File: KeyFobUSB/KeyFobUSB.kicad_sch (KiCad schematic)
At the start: 17 parts, among them J1 USB_A, SW2 SW_SPDT, U1 ATtiny85V-10S

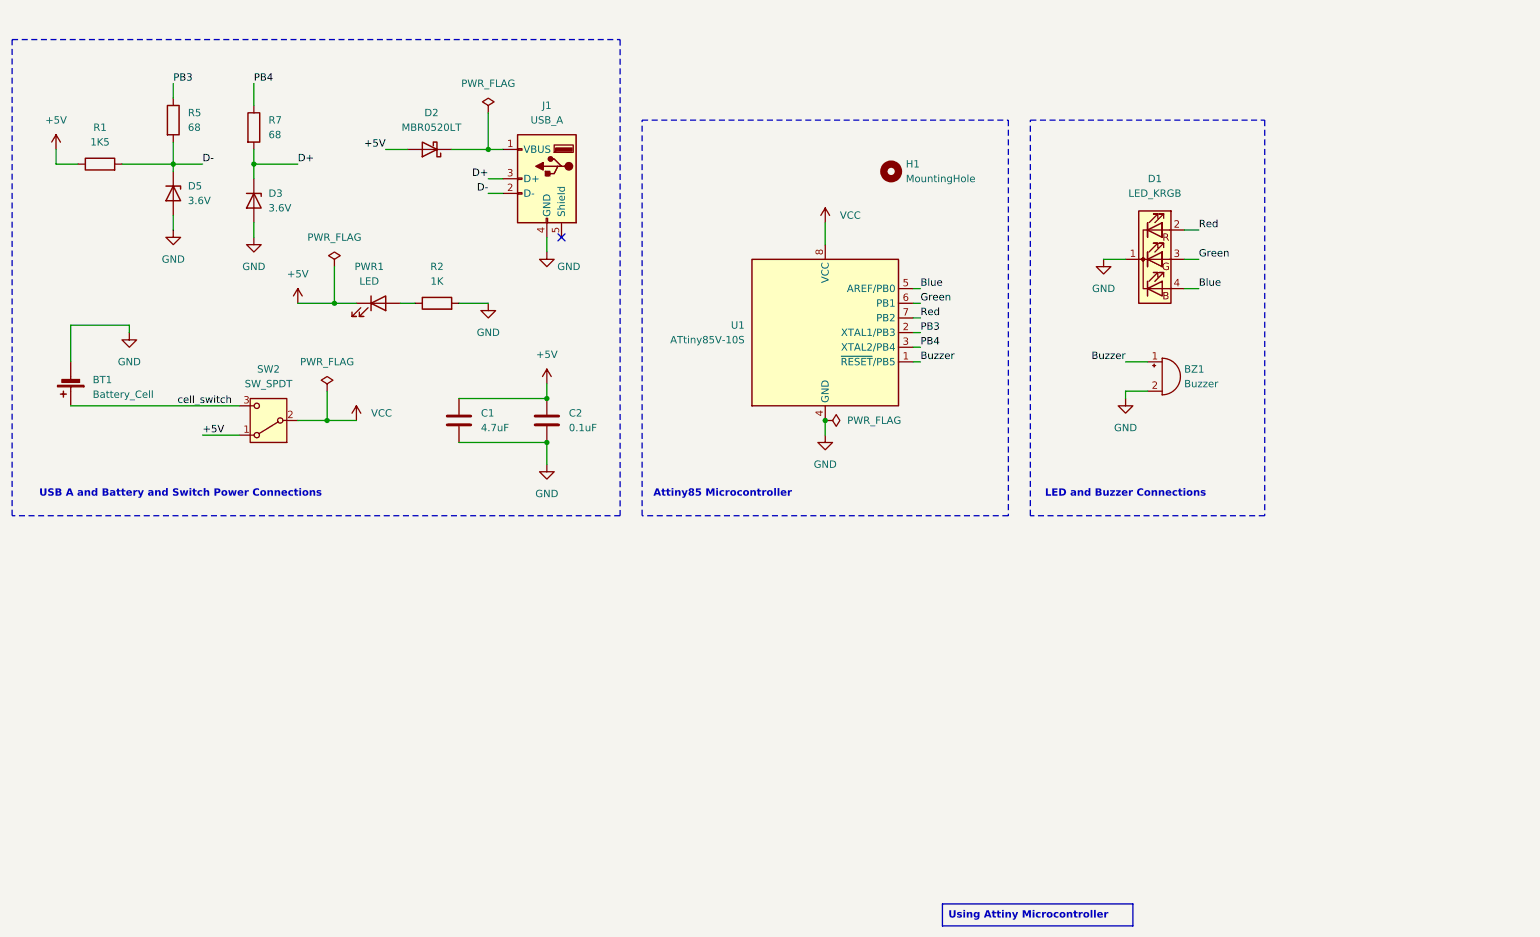
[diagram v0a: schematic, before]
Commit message: Completed the schematic and placed the components on pcb
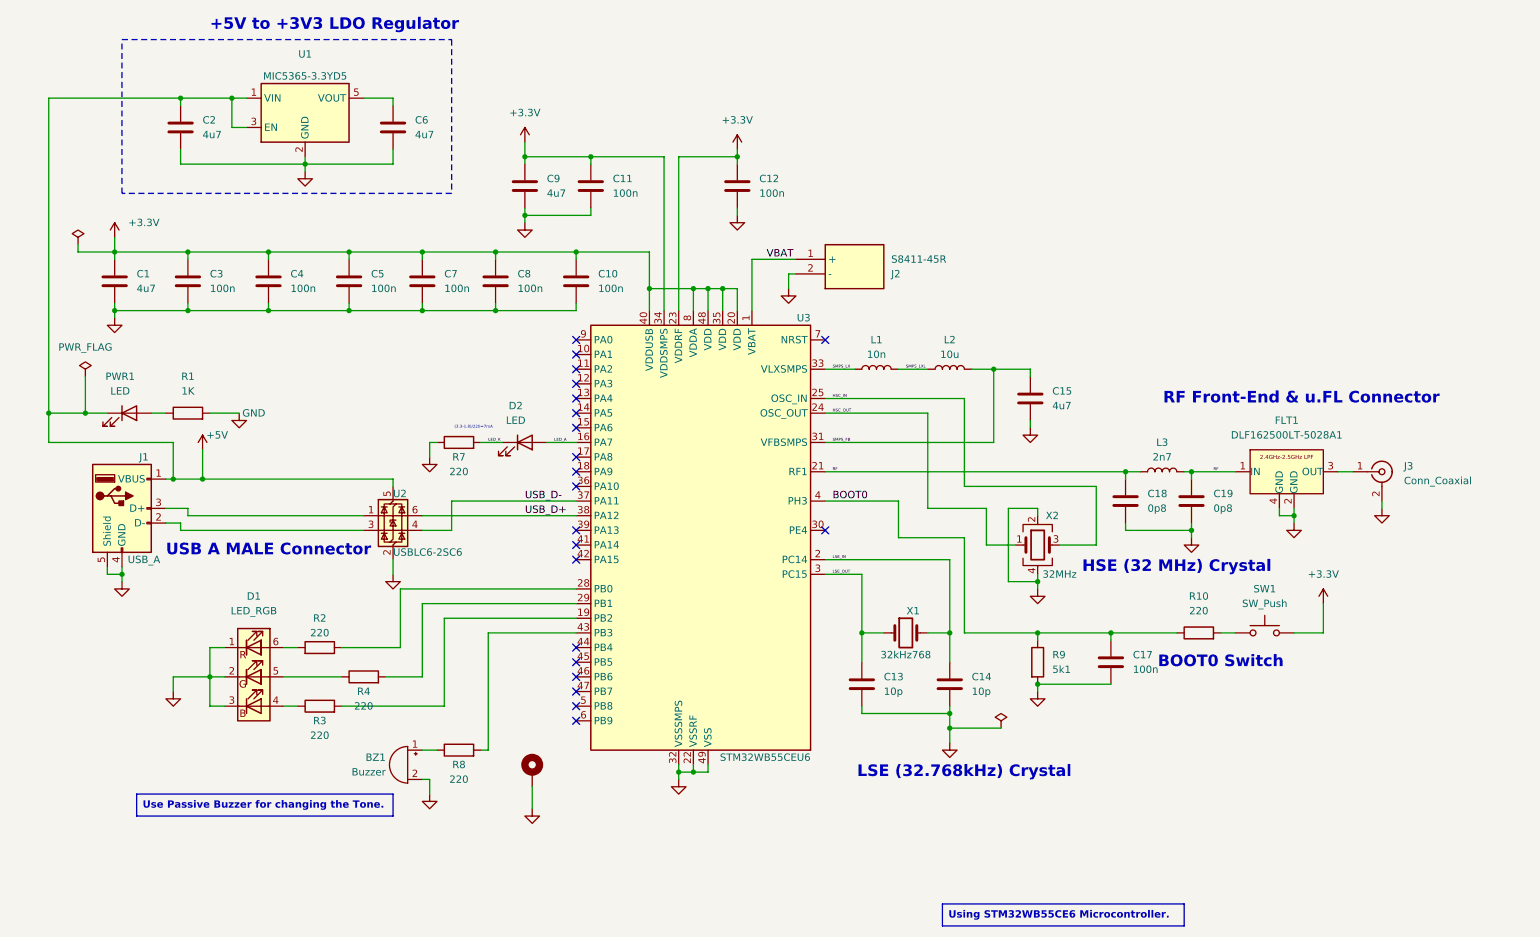
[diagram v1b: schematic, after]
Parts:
- removed BT1: Battery_Cell, 22BatteryHoldercoincell_S8411-45R:S8411-45R_1, symbol Device:Battery_Cell
- removed D1: LED_KRGB, LED_THT:LED_D5.0mm-4_RGB, symbol Device:LED_KRGB
- removed D2: MBR0520LT, Diode_SMD:D_SOD-123, symbol Diode:MBR0520LT
- removed D3, D5: 3.6V, Diode_SMD:D_1206_3216Metric, symbol Device:D_Zener
- removed H1: MountingHole, MountingHole:MountingHole_4.3mm_M4, symbol Mechanical:MountingHole
- removed R1: 1K5, Resistor_SMD:R_0805_2012Metric, symbol Device:R
- removed R5: 68, Resistor_SMD:R_0805_2012Metric, symbol Device:R
- removed SW2: SW_SPDT, Button_Switch_SMD:SW_SPDT_PCM12, symbol Switch:SW_SPDT
- removed U1: ATtiny85V-10S, Package_SO:SOIC-8W_5.3x5.3mm_P1.27mm, symbol MCU_Microchip_ATtiny:ATtiny85V-10S
- added C10, C11, C12, C17, C3, C4, C5, C7, C8: 100n, Capacitor_SMD:C_0805_2012Metric, symbol Device:C
- added C13, C14: 10p, Capacitor_SMD:C_0805_2012Metric, symbol Device:C
- added C15, C6, C9: 4u7, Capacitor_SMD:C_0805_2012Metric, symbol Device:C
- added C18, C19: 0p8, Capacitor_SMD:C_0805_2012Metric, symbol Device:C
- added D1: LED_RGB, LED_SMD:LED_Inolux_IN-P55TATRGB_PLCC6_5.0x5.5mm_P1.8mm, symbol Device:LED_RGB
- added D2: LED, LED_SMD:LED_0805_2012Metric, symbol Device:LED
- added FLT1: DLF162500LT-5028A1, DLF162500LT-5028A1:DLF162500LT-5028A1, symbol STM32withBle_SchematicSymbol:DLF162500LT-5028A1
- added H+1: MountingHole_Pad, MountingHole:MountingHole_3mm_Pad_Via, symbol Mechanical:MountingHole_Pad
- added J2: S8411-45R, 22BatteryHoldercoincell_S8411-45R:S8411-45R_1, symbol battery holder S8411-45R:S8411-45R
- added J3: Conn_Coaxial, Connector_Coaxial:U.FL_Hirose_U.FL-R-SMT-1_Vertical, symbol Connector:Conn_Coaxial
- added L1: 10n, Inductor_SMD:L_0805_2012Metric, symbol Device:L
- added L2: 10u, Inductor_SMD:L_0805_2012Metric, symbol Device:L
- added L3: 2n7, Inductor_SMD:L_0805_2012Metric, symbol Device:L
- added R10, R2, R3, R4, R8: 220, Resistor_SMD:R_0805_2012Metric, symbol Device:R
- added R9: 5k1, Resistor_SMD:R_0805_2012Metric, symbol Device:R
- added SW1: SW_Push, Button_Switch_SMD:SW_SPST_CK_RS282G05A3, symbol Switch:SW_Push
- added U1: MIC5365-3.3YD5, Package_TO_SOT_SMD:SOT-23-5, symbol Regulator_Linear:MIC5365-3.3YD5
- added U2: USBLC6-2SC6, Package_TO_SOT_SMD:SOT-23-6, symbol Power_Protection:USBLC6-2SC6
- added U3: STM32WB55CEU6, Package_DFN_QFN:QFN-48-1EP_7x7mm_P0.5mm_EP5.6x5.6mm, symbol MCU_ST_STM32WB:STM32WB55CEUx
- added X1: 32kHz768, Crystal:Crystal_SMD_2012-2Pin_2.0x1.2mm, symbol Device:Crystal
- added X2: 32MHz, Crystal:Crystal_SMD_2016-4Pin_2.0x1.6mm, symbol Device:Crystal_GND24
- BZ1: footprint Buzzer_Beeper:MagneticBuzzer_ProSignal_ABT-410-RC -> Buzzer_Beeper:Buzzer_CUI_CPT-9019S-SMT
- C1: value 4.7uF -> 4u7
- C2: value 0.1uF -> 4u7
- J1: now left out of the parts list
- R7: value 68 -> 220
- renumbered R2 to R1
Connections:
- net PB4 is gone; now on net GND: R7.1
- net +5V: now also J1.1 (VBUS), U1.1 (VIN), U1.3 (EN), U2.5 (VBUS); no longer C1.1
- net GND: now also J1.5 (Shield), C10.2, C11.2, C12.2, C13.2, C14.2, C15.2, C17.2, C18.2, C19.2, C3.2, C4.2, C5.2, C6.2, C7.2, C8.2, C9.2, D1.1 (RK), D1.2 (GK), D1.3 (BK), FLT1.2 (GND), FLT1.4 (GND), H+1.1, J2.2 (-), J3.2 (Ext), R9.2, U1.2 (GND), U2.2 (GND), U3.22 (VSSRF), U3.32 (VSSSMPS), U3.49 (VSS), X2.2, X2.4
- net Buzzer: no longer names the net of BZ1.1 (+)
- net Buzzer: now also R8.1
- net D+: no longer names the net of J1.3 (D+)
- net D+: now also U2.1 (I/O1); no longer R7.2
- net D-: no longer names the net of J1.2 (D-)
- net D-: now also U2.3 (I/O2)
- new net: D1.4 (BA), R3.1
- new net: D1.5 (GA), R4.1
- new net: D1.6 (RA), R2.2
- new net: R4.2, U3.29 (PB1)
- new net: FLT1.3 (OUT), J3.1 (In)
- new net: C6.1, U1.5 (VOUT)
- new net: R10.2, SW1.1
- new net: R8.2, U3.43 (PB3)
- new net: R2.1, U3.28 (PB0)
- new net: R3.2, U3.19 (PB2)
- new net +3.3V: C1.1, C10.1, C11.1, C12.1, C3.1, C4.1, C5.1, C7.1, C8.1, C9.1, SW1.2, U3.20 (VDD), U3.23 (VDDRF), U3.34 (VDDSMPS), U3.35 (VDD), U3.40 (VDDUSB), U3.48 (VDD), U3.8 (VDDA)
- new net BOOT0: C17.1, R10.1, R9.1, U3.4 (PH3)
- new net HSC_IN: U3.25 (OSC_IN), X2.3
- new net HSC_OUT: U3.24 (OSC_OUT), X2.1
- new net LED_A: D2.2 (A), U3.16 (PA7)
- new net LED_K: D2.1 (K), R7.2
- new net LSE_IN: C14.1, U3.2 (PC14), X1.2
- new net LSE_OUT: C13.1, U3.3 (PC15), X1.1
- new net RF: C18.1, C19.1, FLT1.1 (IN), L3.1, L3.2, U3.21 (RF1)
- new net SMPS_FB: C15.1, L2.2, U3.31 (VFBSMPS)
- new net SMPS_LX: L1.1, U3.33 (VLXSMPS)
- new net SMPS_LXL: L1.2, L2.1
- new net USB_D+: U2.6 (I/O1), U3.38 (PA12)
- new net USB_D-: U2.4 (I/O2), U3.37 (PA11)
- new net VBAT: J2.1 (+), U3.1 (VBAT)
- no-connect marks 1 -> 21
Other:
- note added: "(3.3-1.8)/220=7mA"
- note added: "+5V to +3V3 LDO Regulator"
- note added: "BOOT0 Switch"
- note added: "HSE (32 MHz) Crystal"
- note added: "LSE (32.768kHz) Crystal"
- note added: "RF Front-End & u.FL Connector"
- note added: "USB A MALE Connector"
- note removed: "Attiny85 Microcontroller"
- note removed: "LED and Buzzer Connections"
- note removed: "USB A and Battery and Switch Power Connections"
- moved on the sheet: J1, PWR1, R1

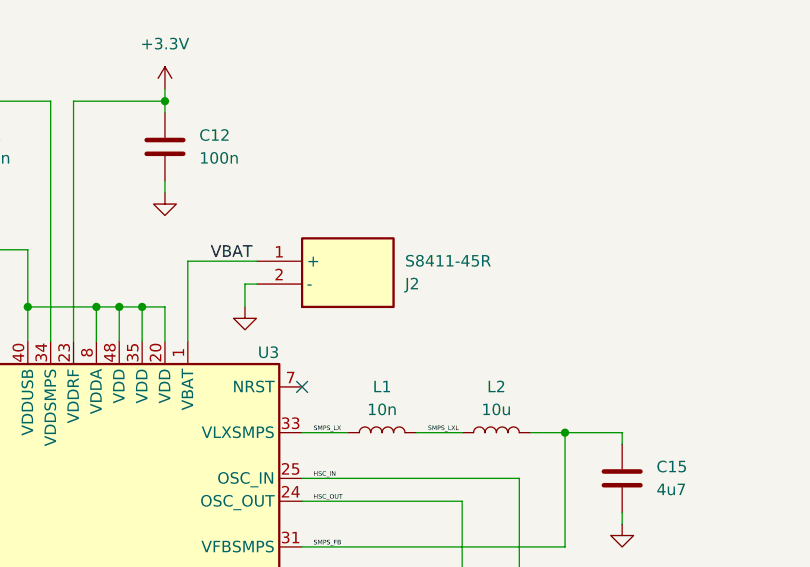
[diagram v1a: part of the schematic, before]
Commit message: added battery holder and vias
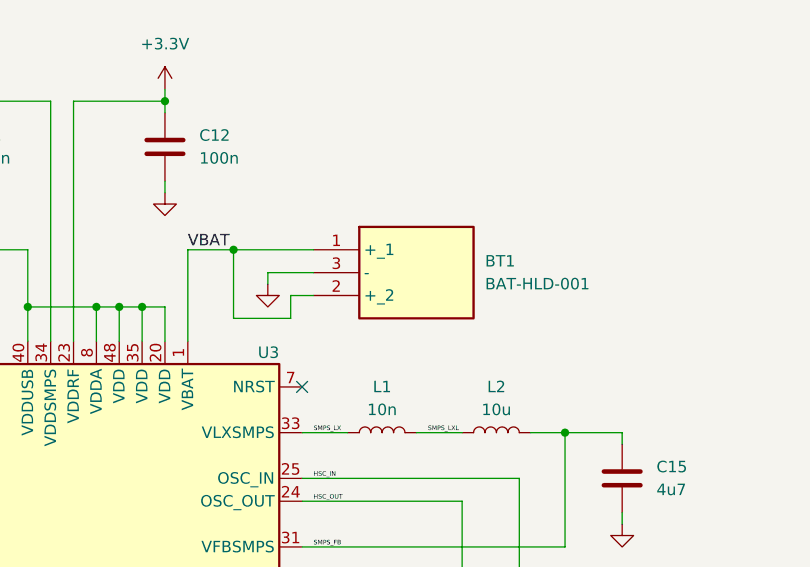
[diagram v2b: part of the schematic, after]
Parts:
- removed J2: S8411-45R, 22BatteryHoldercoincell_S8411-45R:S8411-45R_1, symbol battery holder S8411-45R:S8411-45R
- added BT1: BAT-HLD-001, 22BatteryHoldercoincell_S8411-45R:BATHLD001 CR2032, symbol battery Holder CR2032 001:BAT-HLD-001
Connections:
- net GND: now also BT1.3 (-)
- net VBAT: now also BT1.1 (+_1), BT1.2 (+_2)
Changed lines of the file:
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@@
 	)
 	(junction
+		(at 151.13 54.61)
+		(diameter 0)
+		(color 0 0 0 0)
+	)
+	(junction
 		(at 106.68 38.1)
 		(diameter 0)
@@
 	(wire
 		(pts
-			(xy 146.05 55.88) (xy 146.05 64.77)
+			(xy 146.05 54.61) (xy 146.05 64.77)
 		)
 		(stroke
@@
 	(wire
 		(pts
+			(xy 151.13 62.23) (xy 151.13 54.61)
+		)
+		(stroke
+			(width 0)
+			(type default)
+		)
+	)
+	(wire
+		(pts
 			(xy 88.9 63.5) (xy 88.9 64.77)
 		)
@@
 	(wire
 		(pts
+			(xy 157.48 59.69) (xy 160.02 59.69)
+		)
+		(stroke
+			(width 0)
+			(type default)
+		)
+	)
+	(wire
+		(pts
 			(xy 135.89 60.96) (xy 128.27 60.96)
 		)
@@
 	(wire
 		(pts
-			(xy 153.67 58.42) (xy 152.4 58.42)
+			(xy 154.94 57.15) (xy 160.02 57.15)
 		)
 		(stroke
@@
 	(wire
 		(pts
-			(xy 152.4 58.42) (xy 152.4 60.96)
+			(xy 154.94 57.15) (xy 154.94 58.42)
 		)
 		(stroke
@@
 	(wire
 		(pts
+			(xy 157.48 62.23) (xy 151.13 62.23)
+		)
+		(stroke
+			(width 0)
+			(type default)
+		)
+	)
+	(wire
+		(pts
 			(xy 210.82 93.98) (xy 210.82 92.71)
 		)
@@
 	(wire
 		(pts
+			(xy 151.13 54.61) (xy 160.02 54.61)
+		)
+		(stroke
+			(width 0)
+			(type default)
+		)
+	)
+	(wire
+		(pts
 			(xy 180.34 134.62) (xy 180.34 137.16)
 		)
@@
 	(wire
 		(pts
+			(xy 157.48 59.69) (xy 157.48 62.23)
+		)
+		(stroke
+			(width 0)
+			(type default)
+		)
+	)
+	(wire
+		(pts
 			(xy 52.07 133.35) (xy 52.07 128.27)
 		)
@@
 	(wire
 		(pts
-			(xy 153.67 55.88) (xy 146.05 55.88)
+			(xy 146.05 54.61) (xy 151.13 54.61)
 		)
 		(stroke
@@
 	)
 	(label "VBAT"
-		(at 148.59 55.88 0)
+		(at 146.05 54.61 0)
 		(fields_autoplaced yes)
 		(effects
@@
 	)
 	(symbol
-		(lib_id "battery holder S8411-45R:S8411-45R")
-		(at 153.67 58.42 0)
-		(mirror x)
-		(unit 1)
-		(exclude_from_sim no)
-		(in_bom yes)
-		(on_board yes)
-		(dnp no)
-		(property "Reference" "J2"
-			(at 170.18 58.4201 0)
-			(effects
-				(font
-					(size 1.27 1.27)
-				)
-				(justify left)
-			)
-		)
-		(property "Value" "S8411-45R"
-			(at 170.18 55.8801 0)
-			(effects
-				(font
-					(size 1.27 1.27)
-				)
-				(justify left)
-			)
-		)
-		(property "Footprint" "22BatteryHoldercoincell_S8411-45R:S8411-45R_1"
-			(at 170.18 -36.5 0)
-			(effects
-				(font
-					(size 1.27 1.27)
-				)
-				(justify left top)
-				(hide yes)
-			)
-		)
-		(property "Datasheet" "https://cdn.harwin.com/pdfs/S8411R.pdf"
-			(at 170.18 -136.5 0)
-			(effects
-				(font
-					(size 1.27 1.27)
-				)
-				(justify left top)
-				(hide yes)
-			)
-		)
-		(property "Description" "Coin Cell Battery Retainer, Horizontal SMT, for CR1220 Coin Cell Batteries"
-			(at 153.67 58.42 0)
-			(effects
-				(font
-					(size 1.27 1.27)
-				)
-				(hide yes)
-			)
-		)
-		(property "Height" ""
-			(at 170.18 -336.5 0)
-			(effects
-				(font
-					(size 1.27 1.27)
-				)
-				(justify left top)
-				(hide yes)
-			)
-		)
-		(property "Mouser Part Number" "855-S8411-45R"
-			(at 170.18 -436.5 0)
-			(effects
-				(font
-					(size 1.27 1.27)
-				)
-				(justify left top)
-				(hide yes)
-			)
-		)
-		(property "Mouser Price/Stock" "https://www.mouser.co.uk/ProductDetail/Harwin/S8411-45R?qs=Qom7kyPojXY6B0JhnWxDgQ%3D%3D"
-			(at 170.18 -536.5 0)
-			(effects
-				(font
-					(size 1.27 1.27)
-				)
-				(justify left top)
-				(hide yes)
-			)
-		)
-		(property "Manufacturer_Name" "Harwin"
-			(at 170.18 -636.5 0)
-			(effects
-				(font
-					(size 1.27 1.27)
-				)
-				(justify left top)
-				(hide yes)
-			)
-		)
-		(property "Manufacturer_Part_Number" "S8411-45R"
-			(at 170.18 -736.5 0)
-			(effects
-				(font
-					(size 1.27 1.27)
-				)
-				(justify left top)
-				(hide yes)
-			)
-		)
-		(pin "1"
-		)
-		(pin "2"
-		)
-		(instances
-			(project ""
-				(path "/0fd3cdae-59c4-42b0-a096-27e29e27ac1f"
-					(reference "J2")
-					(unit 1)
-				)
-			)
-		)
-	)
-	(symbol
 		(lib_id "power:GND")
 		(at 195.58 113.03 0)
@@
 	(symbol
 		(lib_id "power:GND")
-		(at 152.4 60.96 0)
+		(at 154.94 58.42 0)
 		(unit 1)
 		(exclude_from_sim no)
@@
 		(fields_autoplaced yes)
 		(property "Reference" "#PWR08"
-			(at 152.4 67.31 0)
+			(at 154.94 64.77 0)
 			(effects
 				(font
@@
 		)
 		(property "Value" "GND"
-			(at 152.4 66.04 0)
+			(at 154.94 63.5 0)
 			(effects
 				(font
@@
 		)
 		(property "Footprint" ""
-			(at 152.4 60.96 0)
+			(at 154.94 58.42 0)
 			(effects
 				(font
@@
 		)
 		(property "Datasheet" ""
-			(at 152.4 60.96 0)
+			(at 154.94 58.42 0)
 			(effects
 				(font
@@
 		)
 		(property "Description" "Power symbol creates a global label with name \"GND\" , ground"
-			(at 152.4 60.96 0)
+			(at 154.94 58.42 0)
 			(effects
 				(font
@@
 					(unit 1)
 				)
+			)
+		)
+	)
+	(symbol
+		(lib_id "battery Holder CR2032 001:BAT-HLD-001")
+		(at 160.02 54.61 0)
+		(unit 1)
+		(exclude_from_sim no)
+		(in_bom yes)
+		(on_board yes)
+		(dnp no)
+		(fields_autoplaced yes)
+		(property "Reference" "BT1"
+			(at 179.07 55.8799 0)
+			(effects
+				(font
+					(size 1.27 1.27)
+				)
+				(justify left)
+			)
+		)
+		(property "Value" "BAT-HLD-001"
+			(at 179.07 58.4199 0)
+			(effects
+				(font
+					(size 1.27 1.27)
+				)
+				(justify left)
+			)
+		)
+		(property "Footprint" "22BatteryHoldercoincell_S8411-45R:BATHLD001 CR2032"
+			(at 179.07 149.53 0)
+			(effects
+				(font
+					(size 1.27 1.27)
+				)
+				(justify left top)
+				(hide yes)
+			)
+		)
+		(property "Datasheet" "https://www.te.com/commerce/DocumentDelivery/DDEController?Action=showdoc&DocId=Customer+Drawing%7FC-BAT-HLD-001-xx%7FE%7Fpdf%7FEnglish%7FENG_CD_C-BAT-HLD-001-xx_E.pdf%7FBAT-HLD-001"
+			(at 179.07 249.53 0)
+			(effects
+				(font
+					(size 1.27 1.27)
+				)
+				(justify left top)
+				(hide yes)
+			)
+		)
+		(property "Description" "Battery Holders, CR2032, 1 Position, Horizontal, Nickel, PCB Mount Alignment, Power, -40  257 F [-40  125 C]"
+			(at 160.02 54.61 0)
+			(effects
+				(font
+					(size 1.27 1.27)
+				)
+				(hide yes)
+			)
+		)
+		(property "Height" "4.3"
+			(at 179.07 449.53 0)
+			(effects
+				(font
+					(size 1.27 1.27)
+				)
+				(justify left top)
+				(hide yes)
+			)
+		)
+		(property "Mouser Part Number" "712-BAT-HLD-001"
+			(at 179.07 549.53 0)
+			(effects
+				(font
+					(size 1.27 1.27)
+				)
+				(justify left top)
+				(hide yes)
+			)
+		)
+		(property "Mouser Price/Stock" "https://www.mouser.co.uk/ProductDetail/TE-Connectivity-Linx-Technologies/BAT-HLD-001?qs=K5ta8V%252BWhta7hbVGfm4dqA%3D%3D"
+			(at 179.07 649.53 0)
+			(effects
+				(font
+					(size 1.27 1.27)
+				)
+				(justify left top)
+				(hide yes)
+			)
+		)
+		(property "Manufacturer_Name" "TE Connectivity"
+			(at 179.07 749.53 0)
+			(effects
+				(font
+					(size 1.27 1.27)
+				)
+				(justify left top)
+				(hide yes)
+			)
+		)
+		(property "Manufacturer_Part_Number" "BAT-HLD-001"
+			(at 179.07 849.53 0)
+			(effects
+				(font
+					(size 1.27 1.27)
+				)
+				(justify left top)
+				(hide yes)
+			)
+		)
+		(pin "2"
+		)
+		(pin "3"
+		)
+		(pin "1"
+		)
+		(instances
+			(project ""
+				(path "/0fd3cdae-59c4-42b0-a096-27e29e27ac1f"
+					(reference "BT1")
+					(unit 1)
+				)
